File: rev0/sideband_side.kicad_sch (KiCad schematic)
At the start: 22 parts, among them IC1 ECP5-BGA256, U8 USB3343-CP

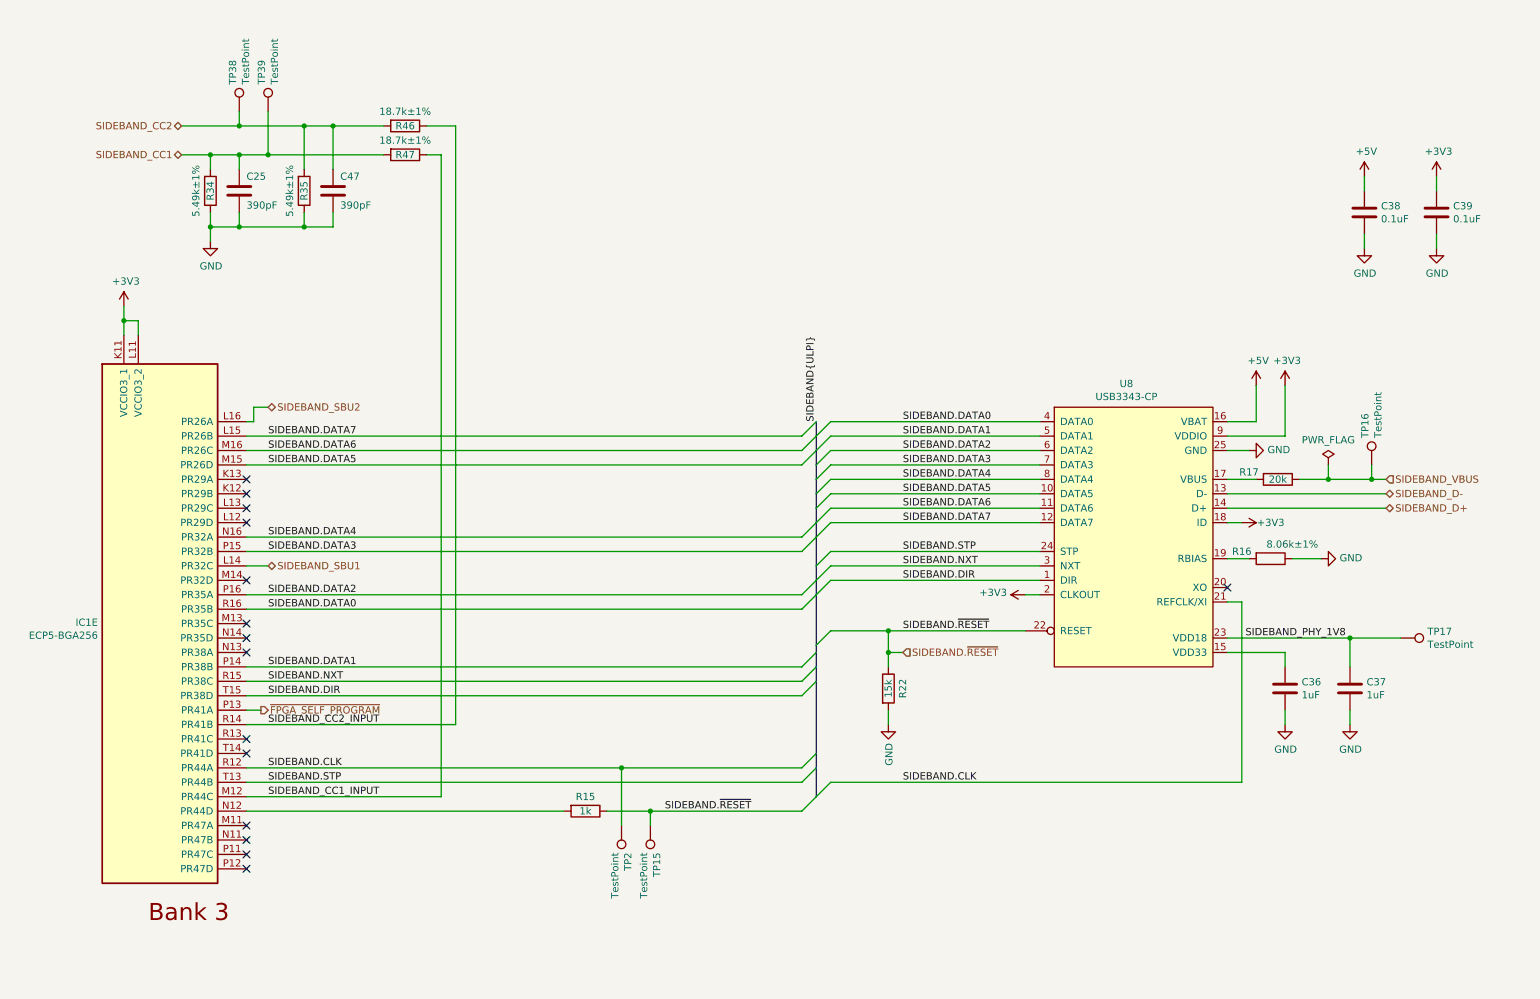
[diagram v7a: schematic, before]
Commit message: hardware: rename USB ports
Sideband is renamed to Control and is intended for use as the primary
control port for both the FPGA and the microcontroller/debugger.

Host is renamed to Aux and is intended for auxiliary functions
including MitM.
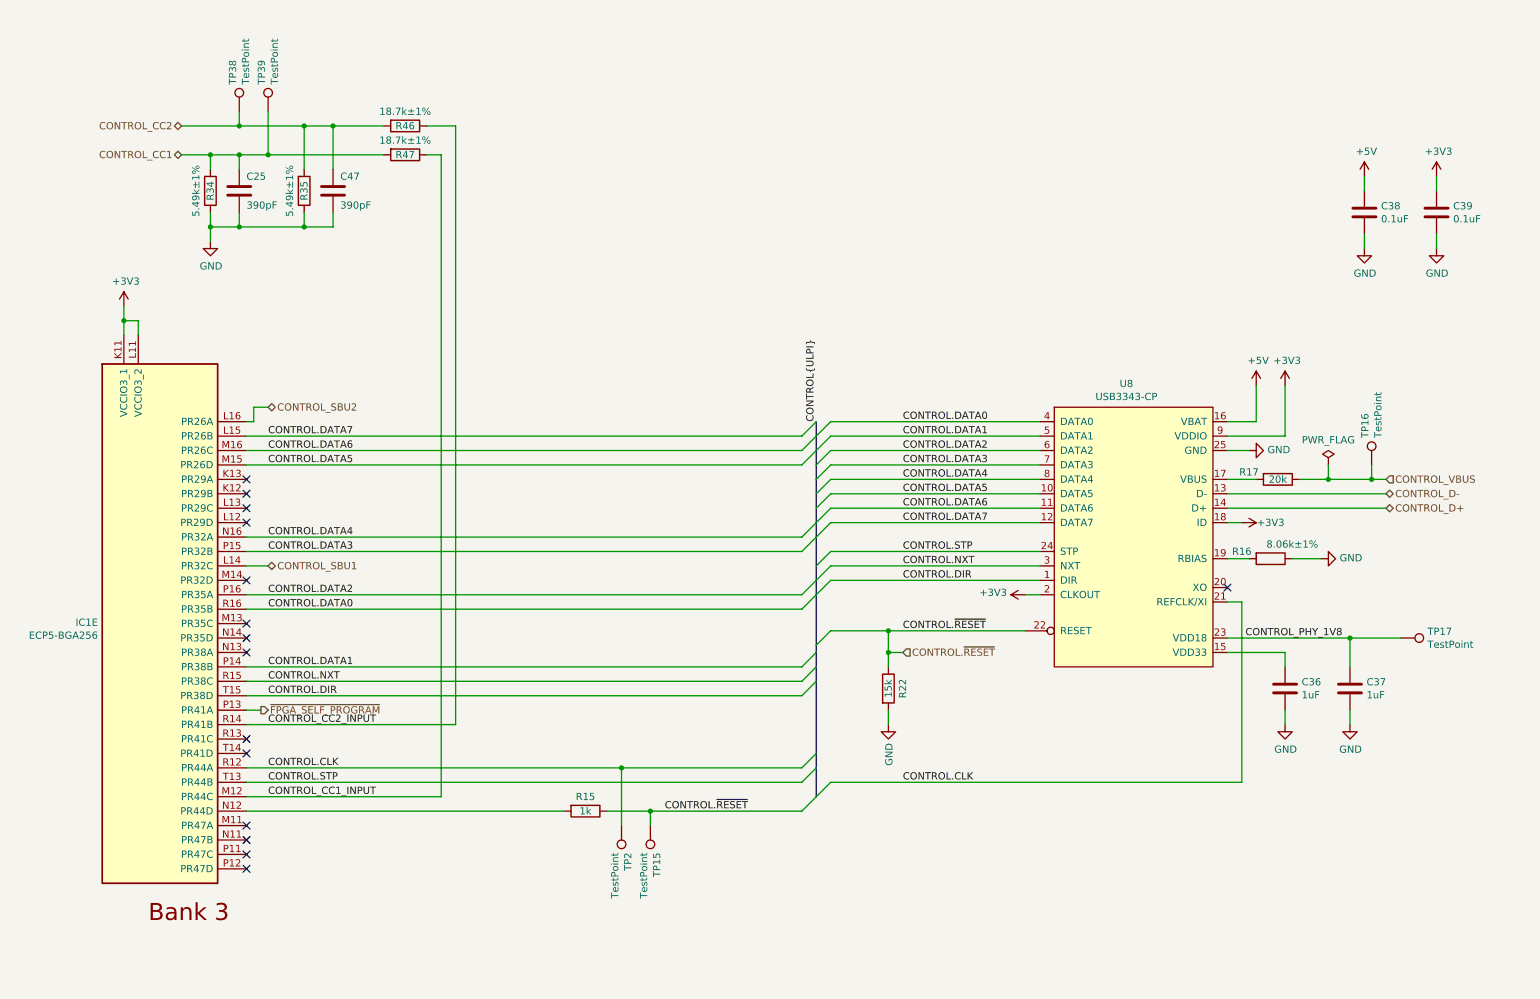
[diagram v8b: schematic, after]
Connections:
- net SIDEBAND.CLK renamed CONTROL.CLK
- net SIDEBAND.DATA0 renamed CONTROL.DATA0
- net SIDEBAND.DATA1 renamed CONTROL.DATA1
- net SIDEBAND.DATA2 renamed CONTROL.DATA2
- net SIDEBAND.DATA3 renamed CONTROL.DATA3
- net SIDEBAND.DATA4 renamed CONTROL.DATA4
- net SIDEBAND.DATA5 renamed CONTROL.DATA5
- net SIDEBAND.DATA6 renamed CONTROL.DATA6
- net SIDEBAND.DATA7 renamed CONTROL.DATA7
- net SIDEBAND.DIR renamed CONTROL.DIR
- net SIDEBAND.NXT renamed CONTROL.NXT
- net SIDEBAND.STP renamed CONTROL.STP
- net SIDEBAND.~{RESET} renamed CONTROL.~{RESET}
- net SIDEBAND_CC1 renamed CONTROL_CC1
- net SIDEBAND_CC1_INPUT renamed CONTROL_CC1_INPUT
- net SIDEBAND_CC2 renamed CONTROL_CC2
- net SIDEBAND_CC2_INPUT renamed CONTROL_CC2_INPUT
- net SIDEBAND_D+ renamed CONTROL_D+
- net SIDEBAND_D- renamed CONTROL_D-
- net SIDEBAND_PHY_1V8 renamed CONTROL_PHY_1V8
- net SIDEBAND_SBU1 renamed CONTROL_SBU1
- net SIDEBAND_SBU2 renamed CONTROL_SBU2
- net SIDEBAND_VBUS renamed CONTROL_VBUS
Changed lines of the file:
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@@
     (stroke (width 0) (type default) (color 0 0 0 0))
   )
-  (label "SIDEBAND.CLK" (at 57.15 147.32 0)
+  (label "CONTROL.CLK" (at 57.15 147.32 0)
     (effects (font (size 1.27 1.27)) (justify left bottom))
   )
-  (label "SIDEBAND.DATA0" (at 57.15 119.38 0)
+  (label "CONTROL.DATA0" (at 57.15 119.38 0)
     (effects (font (size 1.27 1.27)) (justify left bottom))
   )
-  (label "SIDEBAND.DATA5" (at 168.91 99.06 0)
+  (label "CONTROL.DATA5" (at 168.91 99.06 0)
     (effects (font (size 1.27 1.27)) (justify left bottom))
   )
-  (label "SIDEBAND.STP" (at 168.91 109.22 0)
+  (label "CONTROL.STP" (at 168.91 109.22 0)
     (effects (font (size 1.27 1.27)) (justify left bottom))
   )
-  (label "SIDEBAND.DATA2" (at 168.91 91.44 0)
+  (label "CONTROL.DATA2" (at 168.91 91.44 0)
     (effects (font (size 1.27 1.27)) (justify left bottom))
   )
-  (label "SIDEBAND.DIR" (at 168.91 114.3 0)
+  (label "CONTROL.DIR" (at 168.91 114.3 0)
     (effects (font (size 1.27 1.27)) (justify left bottom))
   )
-  (label "SIDEBAND.DATA4" (at 57.15 106.68 0)
+  (label "CONTROL.DATA4" (at 57.15 106.68 0)
     (effects (font (size 1.27 1.27)) (justify left bottom))
   )
-  (label "SIDEBAND.DATA3" (at 168.91 93.98 0)
+  (label "CONTROL.DATA3" (at 168.91 93.98 0)
     (effects (font (size 1.27 1.27)) (justify left bottom))
   )
-  (label "SIDEBAND_PHY_1V8" (at 229.235 124.46 0)
+  (label "CONTROL_PHY_1V8" (at 229.235 124.46 0)
     (effects (font (size 1.27 1.27)) (justify left bottom))
   )
-  (label "SIDEBAND.CLK" (at 168.91 149.86 0)
+  (label "CONTROL.CLK" (at 168.91 149.86 0)
     (effects (font (size 1.27 1.27)) (justify left bottom))
   )
-  (label "SIDEBAND.DATA4" (at 168.91 96.52 0)
+  (label "CONTROL.DATA4" (at 168.91 96.52 0)
     (effects (font (size 1.27 1.27)) (justify left bottom))
   )
-  (label "SIDEBAND.DATA7" (at 57.15 88.9 0)
+  (label "CONTROL.DATA7" (at 57.15 88.9 0)
     (effects (font (size 1.27 1.27)) (justify left bottom))
   )
-  (label "SIDEBAND.DATA2" (at 57.15 116.84 0)
+  (label "CONTROL.DATA2" (at 57.15 116.84 0)
     (effects (font (size 1.27 1.27)) (justify left bottom))
   )
-  (label "SIDEBAND_CC1_INPUT" (at 57.15 152.4 0)
+  (label "CONTROL_CC1_INPUT" (at 57.15 152.4 0)
     (effects (font (size 1.27 1.27)) (justify left bottom))
   )
-  (label "SIDEBAND.DIR" (at 57.15 134.62 0)
+  (label "CONTROL.DIR" (at 57.15 134.62 0)
     (effects (font (size 1.27 1.27)) (justify left bottom))
   )
-  (label "SIDEBAND.DATA1" (at 57.15 129.54 0)
+  (label "CONTROL.DATA1" (at 57.15 129.54 0)
     (effects (font (size 1.27 1.27)) (justify left bottom))
   )
-  (label "SIDEBAND.DATA1" (at 168.91 88.9 0)
+  (label "CONTROL.DATA1" (at 168.91 88.9 0)
     (effects (font (size 1.27 1.27)) (justify left bottom))
   )
-  (label "SIDEBAND.STP" (at 57.15 149.86 0)
+  (label "CONTROL.STP" (at 57.15 149.86 0)
     (effects (font (size 1.27 1.27)) (justify left bottom))
   )
-  (label "SIDEBAND.DATA6" (at 57.15 91.44 0)
+  (label "CONTROL.DATA6" (at 57.15 91.44 0)
     (effects (font (size 1.27 1.27)) (justify left bottom))
   )
-  (label "SIDEBAND{ULPI}" (at 153.67 86.36 90)
+  (label "CONTROL{ULPI}" (at 153.67 86.36 90)
     (effects (font (size 1.27 1.27)) (justify left bottom))
   )
-  (label "SIDEBAND.DATA0" (at 168.91 86.36 0)
+  (label "CONTROL.DATA0" (at 168.91 86.36 0)
     (effects (font (size 1.27 1.27)) (justify left bottom))
   )
-  (label "SIDEBAND.DATA5" (at 57.15 93.98 0)
+  (label "CONTROL.DATA5" (at 57.15 93.98 0)
     (effects (font (size 1.27 1.27)) (justify left bottom))
   )
-  (label "SIDEBAND.NXT" (at 168.91 111.76 0)
+  (label "CONTROL.NXT" (at 168.91 111.76 0)
     (effects (font (size 1.27 1.27)) (justify left bottom))
   )
-  (label "SIDEBAND.DATA6" (at 168.91 101.6 0)
+  (label "CONTROL.DATA6" (at 168.91 101.6 0)
     (effects (font (size 1.27 1.27)) (justify left bottom))
   )
-  (label "SIDEBAND.~{RESET}" (at 168.91 123.19 0)
+  (label "CONTROL.~{RESET}" (at 168.91 123.19 0)
     (effects (font (size 1.27 1.27)) (justify left bottom))
   )
-  (label "SIDEBAND_CC2_INPUT" (at 57.15 139.7 0)
+  (label "CONTROL_CC2_INPUT" (at 57.15 139.7 0)
     (effects (font (size 1.27 1.27)) (justify left bottom))
   )
-  (label "SIDEBAND.NXT" (at 57.15 132.08 0)
+  (label "CONTROL.NXT" (at 57.15 132.08 0)
     (effects (font (size 1.27 1.27)) (justify left bottom))
   )
-  (label "SIDEBAND.~{RESET}" (at 127 154.94 0)
+  (label "CONTROL.~{RESET}" (at 127 154.94 0)
     (effects (font (size 1.27 1.27)) (justify left bottom))
   )
-  (label "SIDEBAND.DATA7" (at 168.91 104.14 0)
+  (label "CONTROL.DATA7" (at 168.91 104.14 0)
     (effects (font (size 1.27 1.27)) (justify left bottom))
   )
-  (label "SIDEBAND.DATA3" (at 57.15 109.22 0)
+  (label "CONTROL.DATA3" (at 57.15 109.22 0)
     (effects (font (size 1.27 1.27)) (justify left bottom))
   )
-  (hierarchical_label "SIDEBAND_VBUS" (shape input) (at 254 96.52 0)
+  (hierarchical_label "CONTROL_VBUS" (shape input) (at 254 96.52 0)
     (effects (font (size 1.27 1.27)) (justify left))
   )
-  (hierarchical_label "SIDEBAND_CC1" (shape bidirectional) (at 41.91 39.37 180)
+  (hierarchical_label "CONTROL_CC1" (shape bidirectional) (at 41.91 39.37 180)
     (effects (font (size 1.27 1.27)) (justify right))
   )
-  (hierarchical_label "SIDEBAND_CC2" (shape bidirectional) (at 41.91 34.29 180)
+  (hierarchical_label "CONTROL_CC2" (shape bidirectional) (at 41.91 34.29 180)
     (effects (font (size 1.27 1.27)) (justify right))
   )
-  (hierarchical_label "SIDEBAND.~{RESET}" (shape input) (at 168.91 127 0)
+  (hierarchical_label "CONTROL.~{RESET}" (shape input) (at 168.91 127 0)
     (effects (font (size 1.27 1.27)) (justify left))
   )
-  (hierarchical_label "SIDEBAND_SBU2" (shape bidirectional) (at 57.15 83.82 0)
+  (hierarchical_label "CONTROL_SBU2" (shape bidirectional) (at 57.15 83.82 0)
     (effects (font (size 1.27 1.27)) (justify left))
   )
@@
     (effects (font (size 1.27 1.27)) (justify left))
   )
-  (hierarchical_label "SIDEBAND_D+" (shape bidirectional) (at 254 101.6 0)
+  (hierarchical_label "CONTROL_D+" (shape bidirectional) (at 254 101.6 0)
     (effects (font (size 1.27 1.27)) (justify left))
   )
-  (hierarchical_label "SIDEBAND_SBU1" (shape bidirectional) (at 57.15 111.76 0)
+  (hierarchical_label "CONTROL_SBU1" (shape bidirectional) (at 57.15 111.76 0)
     (effects (font (size 1.27 1.27)) (justify left))
   )
-  (hierarchical_label "SIDEBAND_D-" (shape bidirectional) (at 254 99.06 0)
+  (hierarchical_label "CONTROL_D-" (shape bidirectional) (at 254 99.06 0)
     (effects (font (size 1.27 1.27)) (justify left))
   )
